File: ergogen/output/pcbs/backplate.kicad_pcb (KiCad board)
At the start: 2 copper layers, 134.2 x 92.7 mm, 0 parts

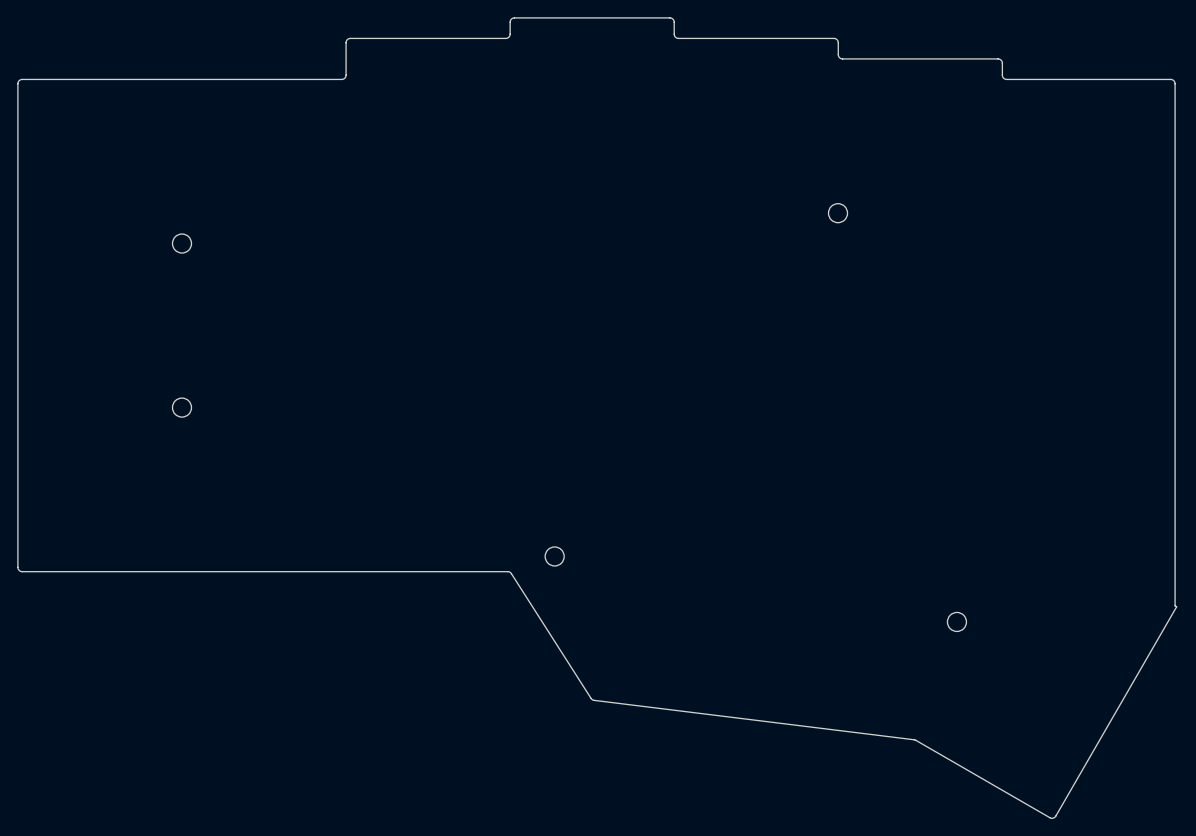
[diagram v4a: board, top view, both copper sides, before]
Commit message: Overhaul outlines making use of intersect
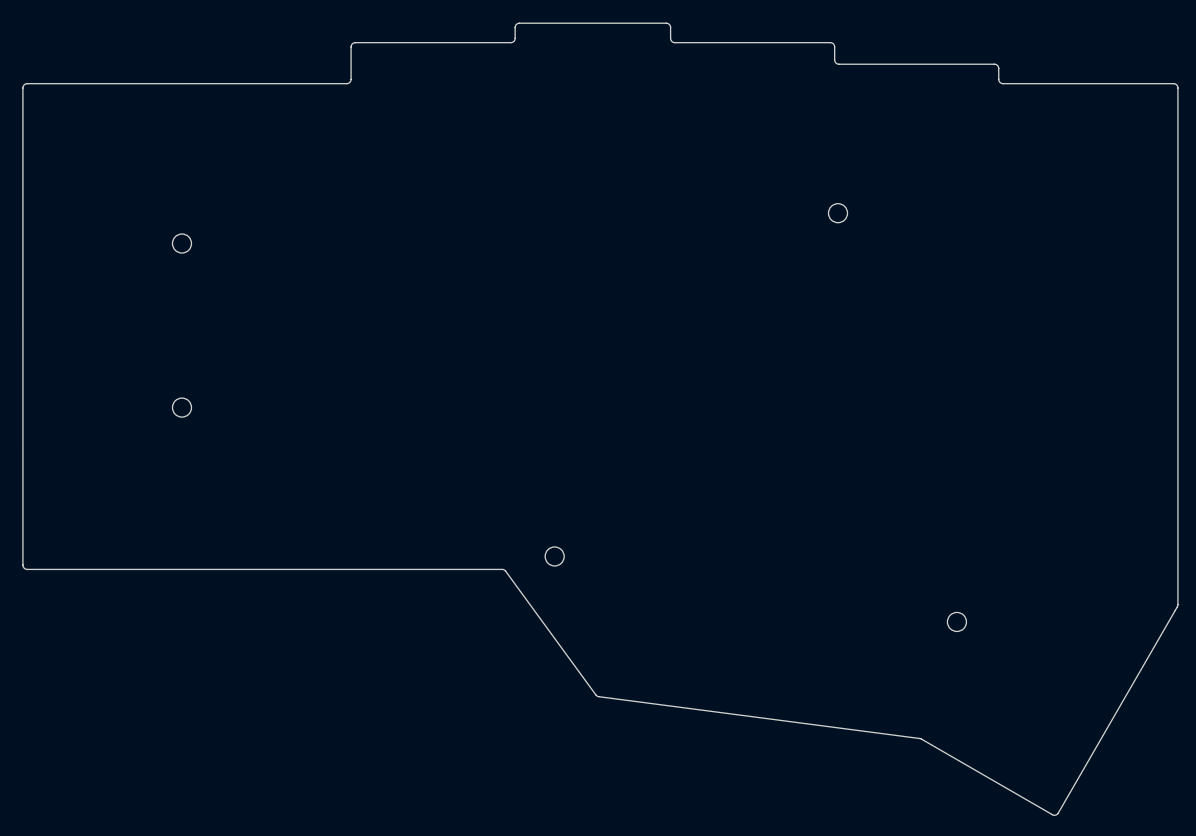
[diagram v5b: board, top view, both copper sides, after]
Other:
- board size 134.2 x 92.7 mm -> 133.8 x 91.7 mm
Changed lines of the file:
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@@
     (add_net "")
   )
-            (gr_line (start 91 109.5) (end 147.226056907563 109.5) (angle 90) (layer Edge.Cuts) (width 0.15))
-(gr_line (start 90.5 109) (end 90.5 53) (angle 90) (layer Edge.Cuts) (width 0.15))
-(gr_line (start 91 52.5) (end 128 52.5) (angle 90) (layer Edge.Cuts) (width 0.15))
-(gr_line (start 147 47.75) (end 129 47.75) (angle 90) (layer Edge.Cuts) (width 0.15))
-(gr_line (start 128.5 48.25) (end 128.5 52) (angle 90) (layer Edge.Cuts) (width 0.15))
-(gr_line (start 166.5 47.25) (end 166.5 45.875) (angle 90) (layer Edge.Cuts) (width 0.15))
-(gr_line (start 166 45.375) (end 148 45.375) (angle 90) (layer Edge.Cuts) (width 0.15))
-(gr_line (start 147.5 45.875) (end 147.5 47.25) (angle 90) (layer Edge.Cuts) (width 0.15))
-(gr_line (start 185.5 49.625) (end 185.5 48.25) (angle 90) (layer Edge.Cuts) (width 0.15))
-(gr_line (start 185 47.75) (end 167 47.75) (angle 90) (layer Edge.Cuts) (width 0.15))
-(gr_line (start 204.5 52) (end 204.5 50.625) (angle 90) (layer Edge.Cuts) (width 0.15))
-(gr_line (start 204 50.125) (end 186 50.125) (angle 90) (layer Edge.Cuts) (width 0.15))
-(gr_line (start 210.68768509880175 137.80950690032108) (end 224.6876851 113.56079560000002) (angle 90) (layer Edge.Cuts) (width 0.15))
-(gr_line (start 224.5 113.45243558639906) (end 224.6876851 113.56079560000002) (angle 90) (layer Edge.Cuts) (width 0.15))
-(gr_line (start 194.4825814717975 129.0308362223767) (end 210.00467239880174 137.99251960032112) (angle 90) (layer Edge.Cuts) (width 0.15))
-(gr_line (start 147.6474496930774 109.73087517731855) (end 156.87331650010177 124.17664030936987) (angle 90) (layer Edge.Cuts) (width 0.15))
-(gr_line (start 157.23359753636308 124.40376678062299) (end 194.2936932210506 128.9675976284421) (angle 90) (layer Edge.Cuts) (width 0.15))
-(gr_line (start 224.5 113.45243558639906) (end 224.5 53) (angle 90) (layer Edge.Cuts) (width 0.15))
-(gr_line (start 224 52.5) (end 205 52.5) (angle 90) (layer Edge.Cuts) (width 0.15))
-(gr_arc (start 147.226056907563 110) (end 147.647449607563 109.7308752) (angle -57.4354397170889) (layer Edge.Cuts) (width 0.15))
-(gr_arc (start 157.2947092856161 123.90751548668835) (end 156.8733165856161 124.17664028668835) (angle -50.414995185869486) (layer Edge.Cuts) (width 0.15))
-(gr_arc (start 194.23258147179752 129.4638489223767) (end 194.48258147179752 129.0308362223767) (angle -22.979555577197353) (layer Edge.Cuts) (width 0.15))
-(gr_arc (start 210.25467239880174 137.5595069003211) (end 210.00467239880174 137.99251960032112) (angle -90.00000000000279) (layer Edge.Cuts) (width 0.15))
-(gr_arc (start 224 53) (end 224.5 53) (angle -90) (layer Edge.Cuts) (width 0.15))
-(gr_arc (start 205 52) (end 204.5 52) (angle -90) (layer Edge.Cuts) (width 0.15))
-(gr_arc (start 204 50.625) (end 204.5 50.625) (angle -90) (layer Edge.Cuts) (width 0.15))
-(gr_arc (start 186 49.625) (end 185.5 49.625) (angle -90) (layer Edge.Cuts) (width 0.15))
-(gr_arc (start 185 48.25) (end 185.5 48.25) (angle -90) (layer Edge.Cuts) (width 0.15))
-(gr_arc (start 167 47.25) (end 166.5 47.25) (angle -90) (layer Edge.Cuts) (width 0.15))
-(gr_arc (start 166 45.875) (end 166.5 45.875) (angle -90) (layer Edge.Cuts) (width 0.15))
-(gr_arc (start 148 45.875) (end 148 45.375) (angle -90) (layer Edge.Cuts) (width 0.15))
-(gr_arc (start 147 47.25) (end 147 47.75) (angle -90) (layer Edge.Cuts) (width 0.15))
-(gr_arc (start 129 48.25) (end 129 47.75) (angle -90) (layer Edge.Cuts) (width 0.15))
-(gr_arc (start 128 52) (end 128 52.5) (angle -90) (layer Edge.Cuts) (width 0.15))
-(gr_arc (start 91 53) (end 91 52.5) (angle -90) (layer Edge.Cuts) (width 0.15))
-(gr_arc (start 91 109) (end 90.5 109) (angle -90) (layer Edge.Cuts) (width 0.15))
+            (gr_line (start 91.08198222285509 108.74001780012622) (end 91.08001777794281 53.49000464193523) (angle 90) (layer Edge.Cuts) (width 0.15))
+(gr_line (start 91.58000462794281 52.98998684198348) (end 128.58001314999998 52.98901315754868) (angle 90) (layer Edge.Cuts) (width 0.15))
+(gr_line (start 129.08 52.48901315754736) (end 129.08 48.74) (angle 90) (layer Edge.Cuts) (width 0.15))
+(gr_line (start 129.58 48.24) (end 147.58 48.24) (angle 90) (layer Edge.Cuts) (width 0.15))
+(gr_line (start 148.08 47.74) (end 148.08 46.488) (angle 90) (layer Edge.Cuts) (width 0.15))
+(gr_line (start 148.58 45.988) (end 165.582 45.988) (angle 90) (layer Edge.Cuts) (width 0.15))
+(gr_line (start 166.082 46.488) (end 166.082 47.74) (angle 90) (layer Edge.Cuts) (width 0.15))
+(gr_line (start 166.582 48.24) (end 184.581 48.24) (angle 90) (layer Edge.Cuts) (width 0.15))
+(gr_line (start 185.081 48.74) (end 185.081 50.238) (angle 90) (layer Edge.Cuts) (width 0.15))
+(gr_line (start 185.581 50.738) (end 203.58222192628773 50.738) (angle 90) (layer Edge.Cuts) (width 0.15))
+(gr_line (start 204.08222192628773 51.23777800000971) (end 204.08277807371226 52.49022199999308) (angle 90) (layer Edge.Cuts) (width 0.15))
+(gr_line (start 224.518 113.996596) (end 210.97353193043912 137.45836746290388) (angle 90) (layer Edge.Cuts) (width 0.15))
+(gr_line (start 210.29050971794075 137.64139668455357) (end 195.12364206223265 128.884801539137) (angle 90) (layer Edge.Cuts) (width 0.15))
+(gr_line (start 194.9382670622326 128.82200823913698) (end 157.77283771855778 123.97774197949536) (angle 90) (layer Edge.Cuts) (width 0.15))
+(gr_line (start 157.43351074236324 123.77659301213079) (end 146.97978450304703 109.44534296736454) (angle 90) (layer Edge.Cuts) (width 0.15))
+(gr_line (start 146.57583252685248 109.24) (end 91.58198222285512 109.24) (angle 90) (layer Edge.Cuts) (width 0.15))
+(gr_line (start 204.58277807371226 52.99) (end 224.333 52.99) (angle 90) (layer Edge.Cuts) (width 0.15))
+(gr_line (start 224.833 53.49) (end 224.833 113.31702540612952) (angle 90) (layer Edge.Cuts) (width 0.15))
+(gr_line (start 224.76601270000006 113.5670254061294) (end 224.518 113.996596) (angle 90) (layer Edge.Cuts) (width 0.15))
+(gr_arc (start 91.58001777794281 53.48998684156686) (end 91.58000457794282 52.98998684156686) (angle -90.00053289295953) (layer Edge.Cuts) (width 0.15))
+(gr_arc (start 128.58 52.48901315754736) (end 128.5800131 52.98901315754736) (angle -89.99849312100235) (layer Edge.Cuts) (width 0.15))
+(gr_arc (start 129.58 48.74) (end 129.58 48.24) (angle -90) (layer Edge.Cuts) (width 0.15))
+(gr_arc (start 147.58 47.74) (end 147.58 48.24) (angle -90) (layer Edge.Cuts) (width 0.15))
+(gr_arc (start 148.58 46.488) (end 148.58 45.988) (angle -90) (layer Edge.Cuts) (width 0.15))
+(gr_arc (start 165.582 46.488) (end 166.082 46.488) (angle -90) (layer Edge.Cuts) (width 0.15))
+(gr_arc (start 166.582 47.74) (end 166.082 47.74) (angle -90) (layer Edge.Cuts) (width 0.15))
+(gr_arc (start 184.581 48.74) (end 185.081 48.74) (angle -90) (layer Edge.Cuts) (width 0.15))
+(gr_arc (start 185.581 50.238) (end 185.081 50.238) (angle -90) (layer Edge.Cuts) (width 0.15))
+(gr_arc (start 203.58222192628773 51.238) (end 204.08222192628773 51.237778) (angle -89.97456067668081) (layer Edge.Cuts) (width 0.15))
+(gr_arc (start 204.58277807371226 52.48999999999069) (end 204.08277807371226 52.49022199999069) (angle -89.97456067529339) (layer Edge.Cuts) (width 0.15))
+(gr_arc (start 224.333 53.49) (end 224.833 53.49) (angle -90) (layer Edge.Cuts) (width 0.15))
+(gr_arc (start 224.333 113.31702540612952) (end 224.7660127 113.56702540612952) (angle -30.000000108401252) (layer Edge.Cuts) (width 0.15))
+(gr_arc (start 210.54050971794078 137.20838398455356) (end 210.29050971794078 137.64139668455357) (angle -90.00218462143252) (layer Edge.Cuts) (width 0.15))
+(gr_arc (start 194.87364206223262 129.31781423913696) (end 195.12364206223262 128.88480153913696) (angle -22.57374496727097) (layer Edge.Cuts) (width 0.15))
+(gr_arc (start 157.83746271855782 123.48193597949538) (end 157.4335107185578 123.77659307949537) (angle -46.46539472382716) (layer Edge.Cuts) (width 0.15))
+(gr_arc (start 146.57583252685248 109.74) (end 146.97978452685248 109.4453429) (angle -53.89164986497705) (layer Edge.Cuts) (width 0.15))
+(gr_arc (start 91.58198222285512 108.74) (end 91.08198222285512 108.74001779999999) (angle -89.99796025578533) (layer Edge.Cuts) (width 0.15))
 (gr_circle (center 109.5 71.5) (end 110.6 71.5) (layer Edge.Cuts) (width 0.15))
 (gr_circle (center 109.5 90.5) (end 110.6 90.5) (layer Edge.Cuts) (width 0.15))

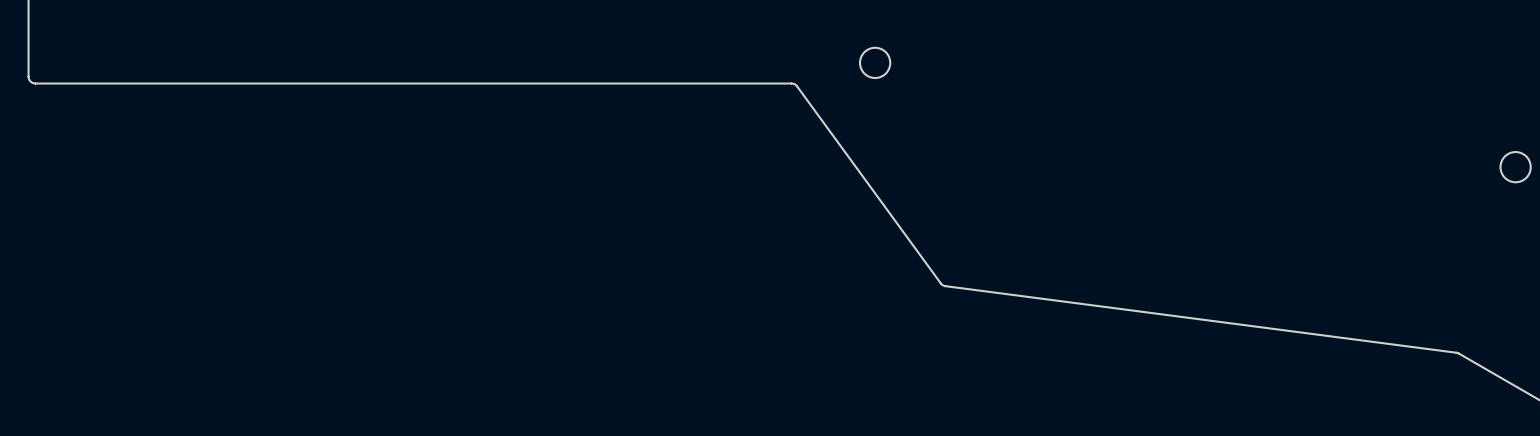
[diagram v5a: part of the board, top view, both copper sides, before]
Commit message: Change to relative measures for helper points
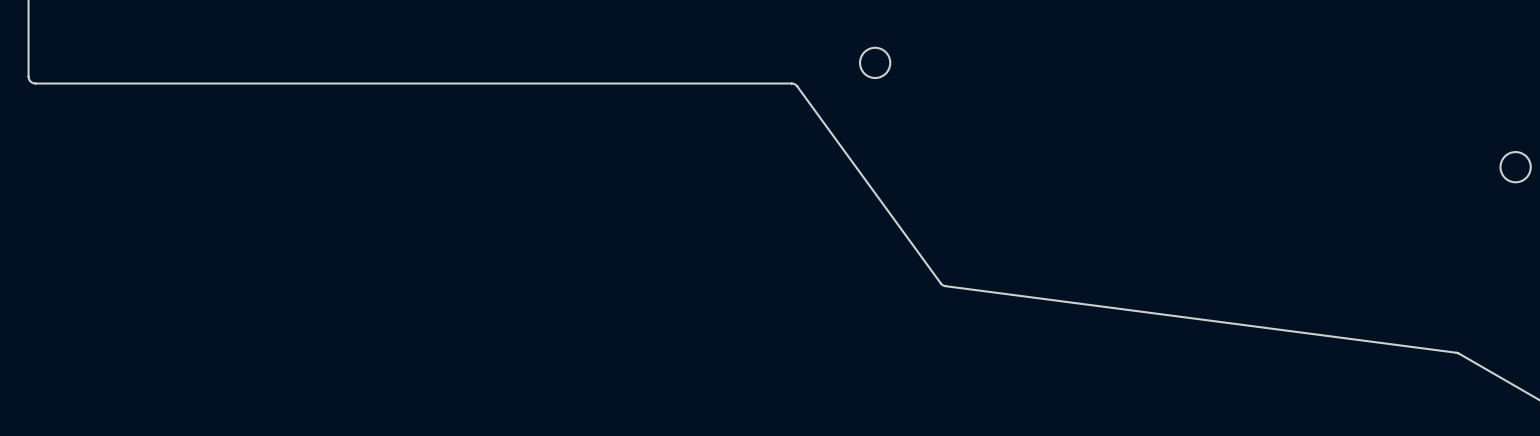
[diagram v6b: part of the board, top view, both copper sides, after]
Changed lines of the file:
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@@
 (gr_line (start 224.518 113.996596) (end 210.97353193043912 137.45836746290388) (angle 90) (layer Edge.Cuts) (width 0.15))
 (gr_line (start 210.29050971794075 137.64139668455357) (end 195.12364206223265 128.884801539137) (angle 90) (layer Edge.Cuts) (width 0.15))
-(gr_line (start 194.9382670622326 128.82200823913698) (end 157.77283771855778 123.97774197949536) (angle 90) (layer Edge.Cuts) (width 0.15))
-(gr_line (start 157.43351074236324 123.77659301213079) (end 146.97978450304703 109.44534296736454) (angle 90) (layer Edge.Cuts) (width 0.15))
-(gr_line (start 146.57583252685248 109.24) (end 91.58198222285512 109.24) (angle 90) (layer Edge.Cuts) (width 0.15))
+(gr_line (start 194.9382670622326 128.82200823913698) (end 157.77296812333506 123.97775897688982) (angle 90) (layer Edge.Cuts) (width 0.15))
+(gr_line (start 157.43351034067848 123.77643070068846) (end 146.98977558129695 109.44552227620129) (angle 90) (layer Edge.Cuts) (width 0.15))
+(gr_line (start 146.5856927986404 109.24) (end 91.58198222285512 109.24) (angle 90) (layer Edge.Cuts) (width 0.15))
 (gr_line (start 204.58277807371226 52.99) (end 224.333 52.99) (angle 90) (layer Edge.Cuts) (width 0.15))
 (gr_line (start 224.833 53.49) (end 224.833 113.31702540612952) (angle 90) (layer Edge.Cuts) (width 0.15))
@@
 (gr_arc (start 210.54050971794078 137.20838398455356) (end 210.29050971794078 137.64139668455357) (angle -90.00218462143252) (layer Edge.Cuts) (width 0.15))
 (gr_arc (start 194.87364206223262 129.31781423913696) (end 195.12364206223262 128.88480153913696) (angle -22.57374496727097) (layer Edge.Cuts) (width 0.15))
-(gr_arc (start 157.83746271855782 123.48193597949538) (end 157.4335107185578 123.77659307949537) (angle -46.46539472382716) (layer Edge.Cuts) (width 0.15))
-(gr_arc (start 146.57583252685248 109.74) (end 146.97978452685248 109.4453429) (angle -53.89164986497705) (layer Edge.Cuts) (width 0.15))
+(gr_arc (start 157.83759312333507 123.48195297688983) (end 157.43351032333507 123.77643067688983) (angle -46.490828368152734) (layer Edge.Cuts) (width 0.15))
+(gr_arc (start 146.5856927986404 109.73999999999998) (end 146.9897755986404 109.44552229999998) (angle -53.917083509298145) (layer Edge.Cuts) (width 0.15))
 (gr_arc (start 91.58198222285512 108.74) (end 91.08198222285512 108.74001779999999) (angle -89.99796025578533) (layer Edge.Cuts) (width 0.15))
 (gr_circle (center 109.5 71.5) (end 110.6 71.5) (layer Edge.Cuts) (width 0.15))

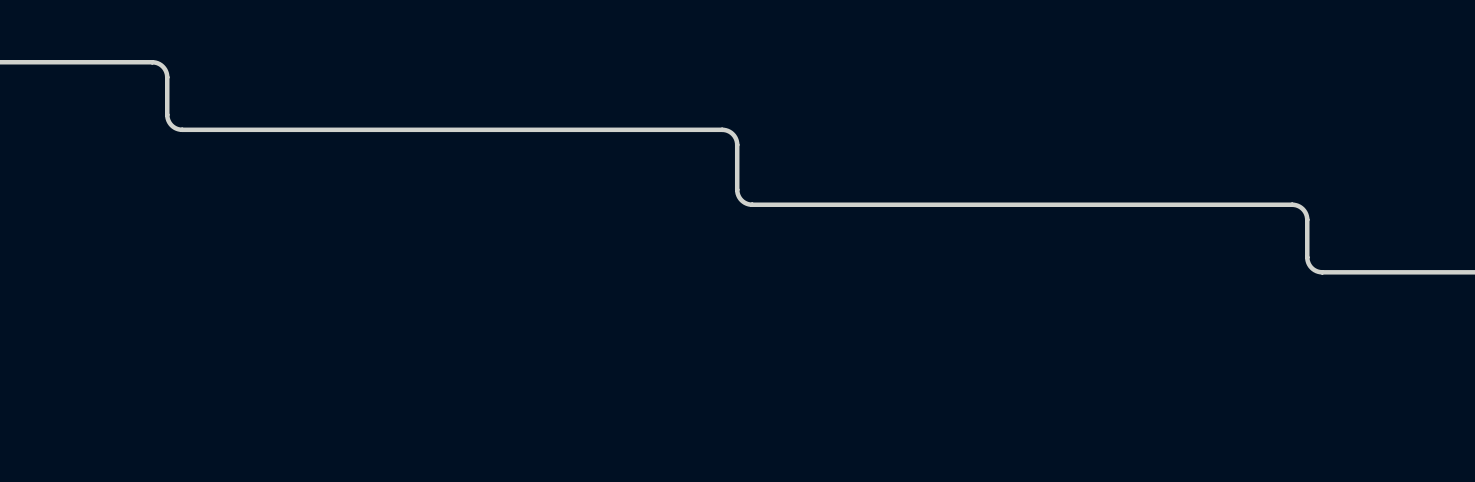
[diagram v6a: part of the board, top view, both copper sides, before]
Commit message: Add missing parametric measures
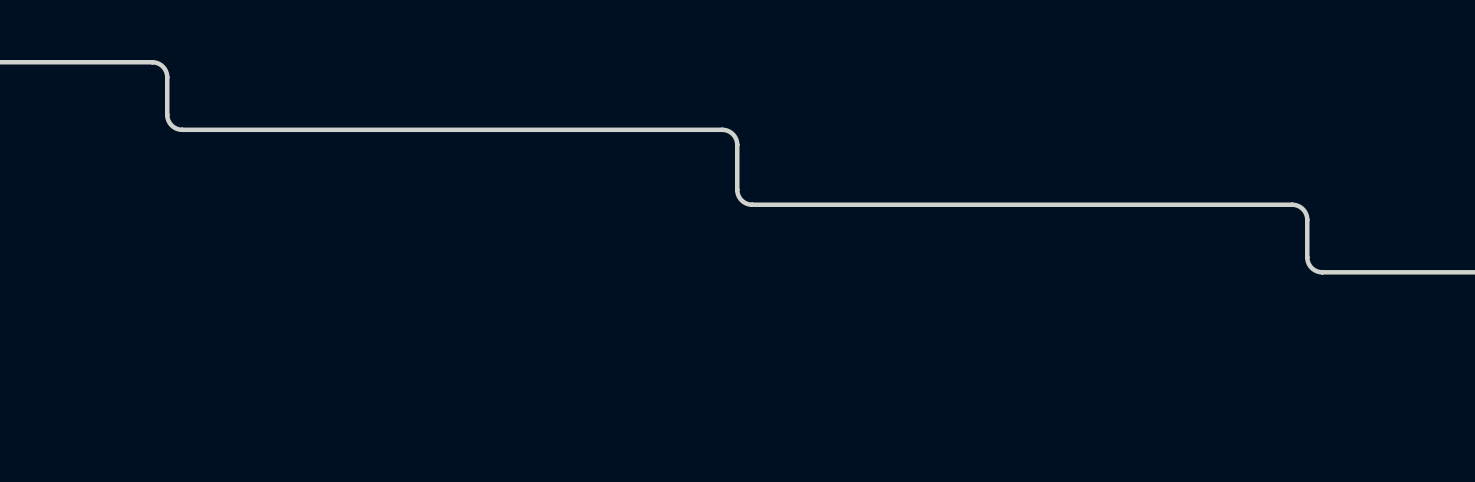
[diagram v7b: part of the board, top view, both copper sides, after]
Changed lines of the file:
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@@
 (gr_line (start 148.58 45.988) (end 165.582 45.988) (angle 90) (layer Edge.Cuts) (width 0.15))
 (gr_line (start 166.082 46.488) (end 166.082 47.74) (angle 90) (layer Edge.Cuts) (width 0.15))
-(gr_line (start 166.582 48.24) (end 184.581 48.24) (angle 90) (layer Edge.Cuts) (width 0.15))
-(gr_line (start 185.081 48.74) (end 185.081 50.238) (angle 90) (layer Edge.Cuts) (width 0.15))
-(gr_line (start 185.581 50.738) (end 203.58222192628773 50.738) (angle 90) (layer Edge.Cuts) (width 0.15))
+(gr_line (start 166.582 48.24) (end 184.582 48.24) (angle 90) (layer Edge.Cuts) (width 0.15))
+(gr_line (start 185.082 48.74) (end 185.082 50.238) (angle 90) (layer Edge.Cuts) (width 0.15))
+(gr_line (start 185.582 50.738) (end 203.58222192628773 50.738) (angle 90) (layer Edge.Cuts) (width 0.15))
 (gr_line (start 204.08222192628773 51.23777800000971) (end 204.08277807371226 52.49022199999308) (angle 90) (layer Edge.Cuts) (width 0.15))
 (gr_line (start 224.518 113.996596) (end 210.97353193043912 137.45836746290388) (angle 90) (layer Edge.Cuts) (width 0.15))
@@
 (gr_arc (start 165.582 46.488) (end 166.082 46.488) (angle -90) (layer Edge.Cuts) (width 0.15))
 (gr_arc (start 166.582 47.74) (end 166.082 47.74) (angle -90) (layer Edge.Cuts) (width 0.15))
-(gr_arc (start 184.581 48.74) (end 185.081 48.74) (angle -90) (layer Edge.Cuts) (width 0.15))
-(gr_arc (start 185.581 50.238) (end 185.081 50.238) (angle -90) (layer Edge.Cuts) (width 0.15))
+(gr_arc (start 184.582 48.74) (end 185.082 48.74) (angle -90) (layer Edge.Cuts) (width 0.15))
+(gr_arc (start 185.582 50.238) (end 185.082 50.238) (angle -90) (layer Edge.Cuts) (width 0.15))
 (gr_arc (start 203.58222192628773 51.238) (end 204.08222192628773 51.237778) (angle -89.97456067668081) (layer Edge.Cuts) (width 0.15))
 (gr_arc (start 204.58277807371226 52.48999999999069) (end 204.08277807371226 52.49022199999069) (angle -89.97456067529339) (layer Edge.Cuts) (width 0.15))
